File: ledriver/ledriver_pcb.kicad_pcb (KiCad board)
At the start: 2 copper layers, 94 x 78.7 mm, 69 parts, among them J1 POT1, J10 USB+-, J11 RX_O_R, J12 REDE_O_R, J13 TX_O_R, J14 dcdc_bypass, J15 dcdc_bypass, J16 DMX, J17 5-12vdc, J18 USB_EXT, J19 M3, J2 POT2, J20 M3, J21 M3, J22 M3, J23 CONN-114-00841-68-MICROSD, J3 RJ2, J4 OLED_I2C, J5 RJ1, J7 Serial2, J8 USB_B, J9 led_out_clk, SW1 SW_SPST, SW2 SW_SPST, SW3 SW_SPST, SW4 SW_SPST, SW5 SW_SPST, U1 MCP1825, U2 WIZ820IO, U3 74HC245, U4 L7805, U5 6N137, U6 6N137, U7 6N137, U8 Teensy3.2, U9 MAX485E

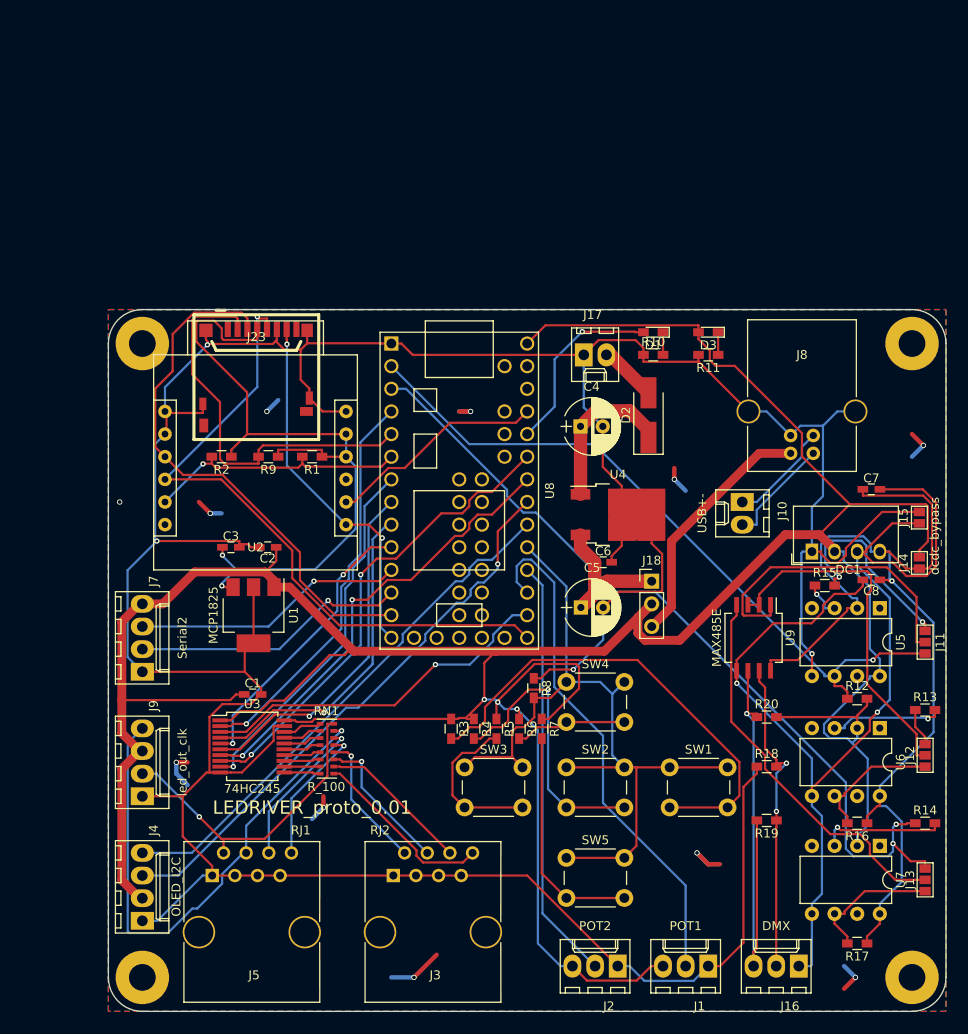
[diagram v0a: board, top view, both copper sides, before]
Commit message: new ledriver layout
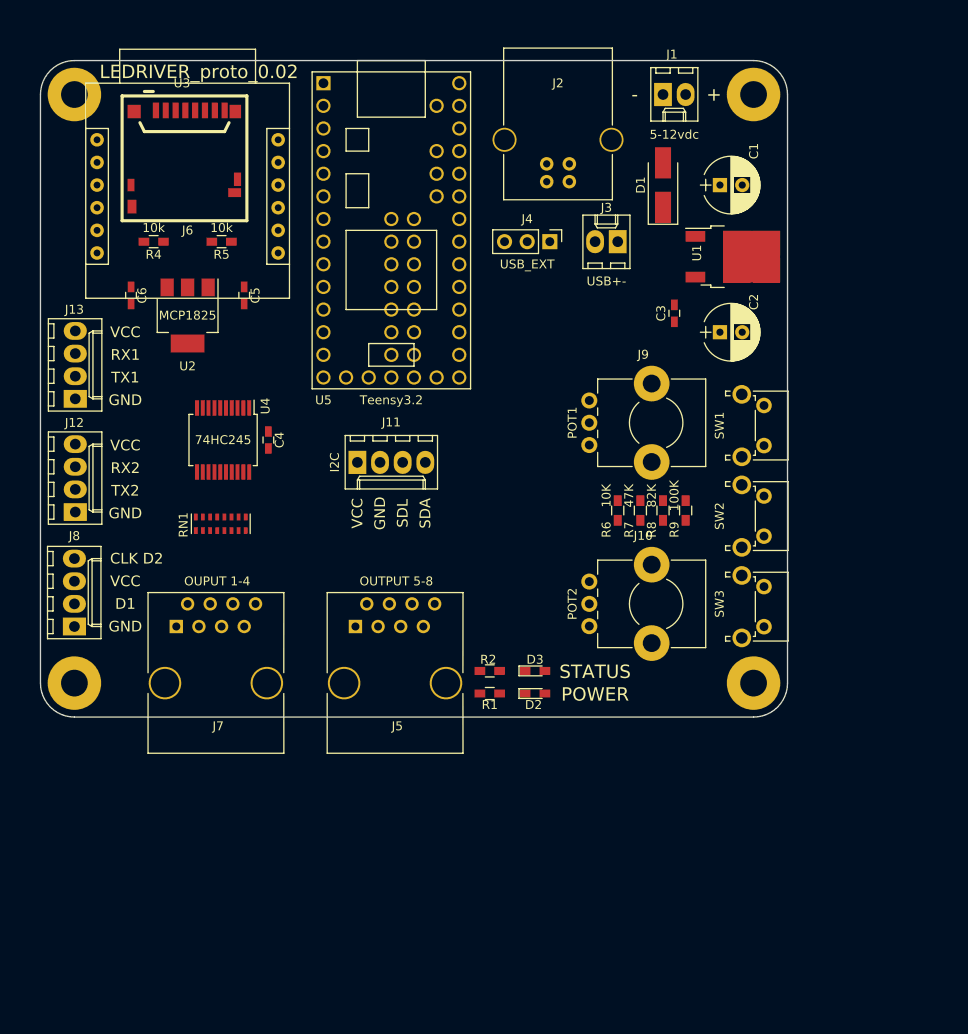
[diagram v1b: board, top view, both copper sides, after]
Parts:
- removed C7, C8: 0.1uF, Capacitors_SMD:C_0603_HandSoldering
- removed DC1: CRE1S0505SC, Converters_DCDC_ACDC:DCDC-Conv_muRata_CRE1xxxxxxSC
- removed J18: USB_EXT, Pin_Headers:Pin_Header_Straight_1x03_Pitch2.54mm
- removed J19, J20, J21, J22: M3, Mounting_Holes:MountingHole_3mm_Pad
- removed J23: CONN-114-00841-68-MICROSD, manuf:AMPHENOL-114-00841-68
- removed R10, R11: 1K, Resistors_SMD:R_0603_HandSoldering
- removed R12, R15: 470, Resistors_SMD:R_0603_HandSoldering
- removed R13, R14: 330, Resistors_SMD:R_0603_HandSoldering
- removed R16, R17: 4.7k, Resistors_SMD:R_0603_HandSoldering
- removed R18, R20: 20K, Resistors_SMD:R_0603_HandSoldering
- removed R19: 120, Resistors_SMD:R_0603_HandSoldering
- removed R3: 10K, Resistors_SMD:R_0603_HandSoldering
- removed SW4, SW5: SW_SPST, Buttons_Switches_THT:SW_PUSH_6mm_h9.5mm
- removed U6, U7: 6N137, Housings_DIP:DIP-8_W7.62mm
- removed U8: Teensy3.2, teensy:Teensy30_31_32_LC
- removed U9: MAX485E, Housings_SOIC:SO-8_5.3x6.2mm_Pitch1.27mm
- added J6: CONN-114-00841-68-MICROSD, manuf:AMPHENOL-114-00841-68, F.Cu at (116.5, 40.8)
- C1: value 1uf -> 47uF; footprint Capacitors_SMD:C_0603_HandSoldering -> Capacitors_THT:CP_Radial_D6.3mm_P2.50mm
- C2: value 0.1uF -> 47uF; footprint Capacitors_SMD:C_0603_HandSoldering -> Capacitors_THT:CP_Radial_D6.3mm_P2.50mm
- C4: value 47uF -> 1uf; footprint Capacitors_THT:CP_Radial_D6.3mm_P2.50mm -> Capacitors_SMD:C_0603_HandSoldering
- C5: value 47uF -> 0.1uF; footprint Capacitors_THT:CP_Radial_D6.3mm_P2.50mm -> Capacitors_SMD:C_0603_HandSoldering
- D1: value LED -> 1N4004; footprint LEDs:LED_0603_HandSoldering -> Diodes_SMD:D_SMA_Handsoldering
- D2: value 1N4004 -> POWER; footprint Diodes_SMD:D_SMA_Handsoldering -> LEDs:LED_0603_HandSoldering
- D3: value POWER -> LED
- J1: value POT1 -> 5-12vdc; footprint Connectors_Molex:Molex_KK-6410-03_03x2.54mm_Straight -> Connectors_Molex:Molex_KK-6410-02_02x2.54mm_Straight
- J10: value USB+- -> POT2; footprint Connectors_Molex:Molex_KK-6410-02_02x2.54mm_Straight -> Potentiometers:Potentiometer_Bourns_PTV09A-1_Horizontal
- J11: value RX_O_R -> I2C; footprint Connectors:GS3 -> Connectors_Molex:Molex_KK-6410-04_04x2.54mm_Straight
- J12: value REDE_O_R -> Serial2; footprint Connectors:GS3 -> Connectors_Molex:Molex_KK-6410-04_04x2.54mm_Straight
- J13: value TX_O_R -> Serial1; footprint Connectors:GS3 -> Connectors_Molex:Molex_KK-6410-04_04x2.54mm_Straight
- J14, J15: value dcdc_bypass -> M3; footprint Connectors:GS2 -> Mounting_Holes:MountingHole_3mm_Pad
- J16: value DMX -> M3; footprint Connectors_Molex:Molex_KK-6410-03_03x2.54mm_Straight -> Mounting_Holes:MountingHole_3mm_Pad
- J17: value 5-12vdc -> M3; footprint Connectors_Molex:Molex_KK-6410-02_02x2.54mm_Straight -> Mounting_Holes:MountingHole_3mm_Pad
- J2: value POT2 -> USB_B; footprint Connectors_Molex:Molex_KK-6410-03_03x2.54mm_Straight -> Connectors:USB_B
- J3: value RJ2 -> USB+-; footprint Connectors:RJ45_8 -> Connectors_Molex:Molex_KK-6410-02_02x2.54mm_Straight
- J4: value OLED_I2C -> USB_EXT; footprint Connectors_Molex:Molex_KK-6410-04_04x2.54mm_Straight -> Pin_Headers:Pin_Header_Straight_1x03_Pitch2.54mm
- J5: value RJ1 -> OUTPUT 5-8; footprint Connectors:RJ45_8 -> robocut_footprint:RJ45_8_54602-908LF
- J7: value Serial2 -> OUPUT 1-4; footprint Connectors_Molex:Molex_KK-6410-04_04x2.54mm_Straight -> robocut_footprint:RJ45_8_54602-908LF
- J8: value USB_B -> led_out_clk; footprint Connectors:USB_B -> Connectors_Molex:Molex_KK-6410-04_04x2.54mm_Straight
- J9: value led_out_clk -> POT1; footprint Connectors_Molex:Molex_KK-6410-04_04x2.54mm_Straight -> Potentiometers:Potentiometer_Bourns_PTV09A-1_Horizontal
- R1, R2: value 10k -> 1K
- R4: value 22K -> 10k
- R5: value 47K -> 10k
- R6: value 68K -> 10K
- R7: value 82K -> 47K
- R8: value 100K -> 82K
- R9: value 10k -> 100K
- SW1, SW2, SW3: footprint Buttons_Switches_THT:SW_PUSH_6mm_h9.5mm -> Buttons_Switches_THT:SW_Tactile_SPST_Angled_PTS645Vx39-2LFS
- U1: value MCP1825 -> L7805; footprint TO_SOT_Packages_SMD:SOT-223-3_TabPin2 -> TO_SOT_Packages_SMD:TO-252-2
- U2: value WIZ820IO -> MCP1825; footprint robocut_footprint:WIZ820IO -> TO_SOT_Packages_SMD:SOT-223-3_TabPin2
- U3: value 74HC245 -> WIZ820IO; footprint Housings_SSOP:SSOP-20_5.3x7.2mm_Pitch0.65mm -> robocut_footprint:WIZ820IO
- U4: value L7805 -> 74HC245; footprint TO_SOT_Packages_SMD:TO-252-2 -> Housings_SSOP:SSOP-20_5.3x7.2mm_Pitch0.65mm
- U5: value 6N137 -> Teensy3.2; footprint Housings_DIP:DIP-8_W7.62mm -> teensy:Teensy30_31_32_LC
- moved J13 109.6 mm to (104.2, 72.2), turned to 90 degrees
- moved J15 106.0 mm to (104.1, 38.1), turned to 0 degrees
- moved J12 99.2 mm to (104.2, 84.9), turned to 90 degrees
- moved J1 97.9 mm to (170.2, 38.1), turned to 0 degrees
- moved J4 88.9 mm to (157.5, 54.6), turned to 270 degrees
- moved J2 88.4 mm to (157.1, 47.9), turned to 90 degrees
- moved J16 87.3 mm to (104.1, 104.1), turned to 0 degrees
- moved J8 82.7 mm to (104.1, 97.8)
- moved C1 77.6 mm to (176.6, 48.3)
- moved J3 75.4 mm to (165.1, 54.6), turned to 180 degrees
- moved U5 69.3 mm to (139.7, 53.3)
- moved U1 67.2 mm to (178.0, 56.3), turned to 0 degrees
- moved J11 66.8 mm to (135.9, 79.4), turned to 0 degrees
- moved R4 65.4 mm to (113.0, 54.6), turned to 180 degrees
- moved J9 63.8 mm to (161.9, 77.4), turned to 0 degrees
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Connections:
- C1 pad 1: VCC -> Net-(C1-Pad1)
- C2 pad 1: VCC -> Net-(C2-Pad1)
- C3 pad 1: Net-(C3-Pad1) -> Net-(C2-Pad1)
- C4 pad 1: Net-(C4-Pad1) -> VCC
- C5 pad 1: Net-(C5-Pad1) -> VCC
- C6 pad 1: Net-(C5-Pad1) -> Net-(C6-Pad1)
- D1 pad 1: Net-(D1-Pad1) -> Net-(C1-Pad1)
- D1 pad 2: /STATUS -> +12V
- D2 pad 1: Net-(C4-Pad1) -> Net-(D2-Pad1)
- D2 pad 2: +12V -> VCC
- D3 pad 2: VCC -> /STATUS
- J1 pad 2: /POT1 -> +12V
- J10 pad 1: Net-(J10-Pad1) -> GND
- J10 pad 2: Net-(J10-Pad2) -> /POT2
- J11 pad 1: /RX1 -> VCC
- J11 pad 2: Net-(J11-Pad2) -> GND
- J11 pad 3: Net-(J11-Pad3) -> /I2C_SCL
- J12 pad 1: /DMX_REDE -> GND
- J12 pad 2: Net-(J12-Pad2) -> /TX2
- J12 pad 3: Net-(J12-Pad3) -> /RX2
- J13 pad 1: /TX1 -> GND
- J13 pad 2: Net-(J13-Pad2) -> /TX1
- J13 pad 3: Net-(J13-Pad3) -> /RX1
- J14 pad 1: VDD -> (no net)
- J15 pad 1: GNDS -> (no net)
- J16 pad 1: GNDS -> (no net)
- J17 pad 1: GND -> (no net)
- J2 pad 1: GND -> Net-(J2-Pad1)
- J2 pad 2: /POT2 -> Net-(J2-Pad2)
- J2 pad 3: VCC -> Net-(J2-Pad3)
- J3 pad 1: GND -> Net-(J2-Pad2)
- J3 pad 2: Net-(J3-Pad2) -> Net-(J2-Pad3)
- J4 pad 1: GND -> Net-(C2-Pad1)
- J4 pad 3: /I2C_SCL -> Net-(J2-Pad1)
- J7 pad 2: /TX2 -> Net-(J7-Pad2)
- J7 pad 3: /RX2 -> GND
- J7 pad 4: VCC -> Net-(J7-Pad4)
- J8 pad 1: Net-(J18-Pad3) -> GND
- J8 pad 2: Net-(J10-Pad2) -> Net-(J7-Pad2)
- J8 pad 3: Net-(J10-Pad1) -> VCC
- J8 pad 4: GND -> Net-(J7-Pad4)
- J9 pad 2: Net-(J5-Pad2) -> /POT1
- R1 pad 1: Net-(C3-Pad1) -> Net-(D2-Pad1)
- R1 pad 2: /SPI_CS_WIZ -> GND
- R2 pad 1: Net-(C3-Pad1) -> GND
- R2 pad 2: /SPI_CS_WIZ -> Net-(D3-Pad1)
- R4 pad 1: VCC -> Net-(C6-Pad1)
- R4 pad 2: Net-(R4-Pad2) -> /SPI_CS_WIZ
- R5 pad 1: VCC -> Net-(C6-Pad1)
- R5 pad 2: Net-(R5-Pad2) -> /SPI_CS_SDCARD
- R8 pad 1: GND -> VCC
- R8 pad 2: /BUTTONS -> Net-(R8-Pad2)
- R9 pad 1: Net-(C3-Pad1) -> GND
- R9 pad 2: /SPI_CS_SDCARD -> /BUTTONS
- RN1 pad 10: Net-(J3-Pad6) -> Net-(J5-Pad6)
- RN1 pad 11: Net-(J3-Pad4) -> Net-(J5-Pad4)
- RN1 pad 12: Net-(J3-Pad2) -> Net-(J5-Pad2)
- RN1 pad 13: Net-(J5-Pad8) -> Net-(J7-Pad8)
- RN1 pad 14: Net-(J5-Pad6) -> Net-(J7-Pad6)
- RN1 pad 15: Net-(J5-Pad4) -> Net-(J7-Pad4)
- RN1 pad 16: Net-(J5-Pad2) -> Net-(J7-Pad2)
- RN1 pad 9: Net-(J3-Pad8) -> Net-(J5-Pad8)
- SW1 pad 2: Net-(R3-Pad2) -> Net-(R6-Pad2)
- SW2 pad 2: Net-(R4-Pad2) -> Net-(R7-Pad2)
- SW3 pad 2: Net-(R5-Pad2) -> Net-(R8-Pad2)
- U1 pad 1: VCC -> Net-(C1-Pad1)
- U1 pad 3: Net-(C3-Pad1) -> Net-(C2-Pad1)
- U2 pad 1: GND -> VCC
- U2 pad 3: /SPI_DOUT -> Net-(C6-Pad1)
- U3 pad 1: VCC -> GND
- U3 pad 10: GND -> Net-(C6-Pad1)
- U3 pad 11: Net-(RN1-Pad8) -> Net-(C6-Pad1)
- U3 pad 12: Net-(RN1-Pad7) -> GND
- U3 pad 2: /DATA_1_PIN_2 -> GND
- U3 pad 3: /DATA_2_PIN_14 -> /SPI_DOUT
- U3 pad 4: /DATA_3_PIN_7 -> /SPI_SCK
- U3 pad 5: /DATA_4_PIN_8 -> /SPI_CS_WIZ
- U3 pad 6: /DATA_5_PIN_6 -> (no net)
- U3 pad 7: /DATA_6_PIN_20 -> /SPI_DIN
- U3 pad 8: /DATA_7_PIN_21 -> /WIZ_RESET
- U3 pad 9: /DATA_8_PIN_5 -> (no net)
- U4 pad 1: Net-(C4-Pad1) -> VCC
- U4 pad 2: GND -> /DATA_1_PIN_2
- U4 pad 3: Net-(C5-Pad1) -> /DATA_2_PIN_14
- U5 pad 1: (no net) -> GND
- U5 pad 2: VDD -> /RX1
- U5 pad 3: Net-(R15-Pad1) -> /TX1
- U5 pad 4: (no net) -> /DATA_1_PIN_2
- U5 pad 5: GND -> /SPI_CS_SDCARD
- U5 pad 6: /RX1 -> /SPI_CS_WIZ
- U5 pad 7: (no net) -> /DATA_8_PIN_5
- U5 pad 8: VCC -> /DATA_5_PIN_6
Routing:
- net GND: track 426.9 -> 0.00 mm, vias 4 -> 0
- net VCC: track 395.8 -> 0.00 mm, vias 3 -> 0
- net GNDS: track 124.0 -> 0.00 mm, vias 2 -> 0
- net VDD: track 111.2 -> 0.00 mm, vias 1 -> 0
- net /TX1: track 93.6 -> 0.00 mm, vias 2 -> 0
- net /BUTTONS: track 88.7 -> 0.00 mm
- net Net-(C3-Pad1): track 81.4 -> 0.00 mm, vias 2 -> 0
- net /RX1: track 79.6 -> 0.00 mm, vias 1 -> 0
- net /SPI_SCK: track 74.8 -> 0.00 mm, vias 1 -> 0
- net /I2C_SCL: track 63.8 -> 0.00 mm, vias 1 -> 0
- net /SPI_DOUT: track 60.5 -> 0.00 mm
- net Net-(J5-Pad4): track 60.2 -> 0.00 mm, vias 1 -> 0
- net /I2C_SDA: track 59.3 -> 0.00 mm
- net /POT1: track 58.2 -> 0.00 mm
- net Net-(R3-Pad2): track 53.8 -> 0.00 mm
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- removed copper zone on B.Cu, net GND
- removed copper zone on F.Cu, net GND
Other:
- board size 94 x 78.7 mm -> 83.8 x 73.7 mm
- board text added: "+"
- board text added: "-"
- board text added: "CLK D2"
- board text added: "D1"
- board text added: "GND"
- board text added: "LEDRIVER_proto_0.02"
- board text added: "POWER"
- board text added: "RX1"
- board text added: "RX2"
- board text added: "SDA"
- board text added: "SDL"
- board text added: "STATUS"
- board text added: "TX1"
- board text added: "TX2"
- board text added: "VCC"
- board text removed: "LEDRIVER_proto_0.01"

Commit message: board detween v02 and v03
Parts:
- J5: value OUTPUT 5-8 -> RJ2
- J7: value OUPUT 1-4 -> RJ1
- moved J11 7.62 mm to (143.5, 79.4), turned to 180 degrees
- moved J6 4.28 mm to (116.5, 36.5)
- moved J2 3.34 mm to (157.1, 44.5)
- moved R4 1.28 mm to (113.0, 53.3)
- moved R5 1.28 mm to (120.7, 53.3)
- moved U4 0.65 mm to (120.2, 76.9)
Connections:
- J11 pad 1: VCC -> /I2C_SDA
- J11 pad 2: GND -> /I2C_SCL
- J11 pad 3: /I2C_SCL -> GND
- J11 pad 4: /I2C_SDA -> VCC
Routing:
- added copper zone on B.Cu, net GND
- added copper zone on F.Cu, net GND
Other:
- board text added: "sdcard move up"
